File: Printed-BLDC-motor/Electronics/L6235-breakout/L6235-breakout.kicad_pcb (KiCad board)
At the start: 2 copper layers, 55 x 43 mm, 35 parts, among them J1 Conn_01x06_Male, J2 HALL, J3 MOTOR, J5 PWR, U1 L6235PD, U2 L7805

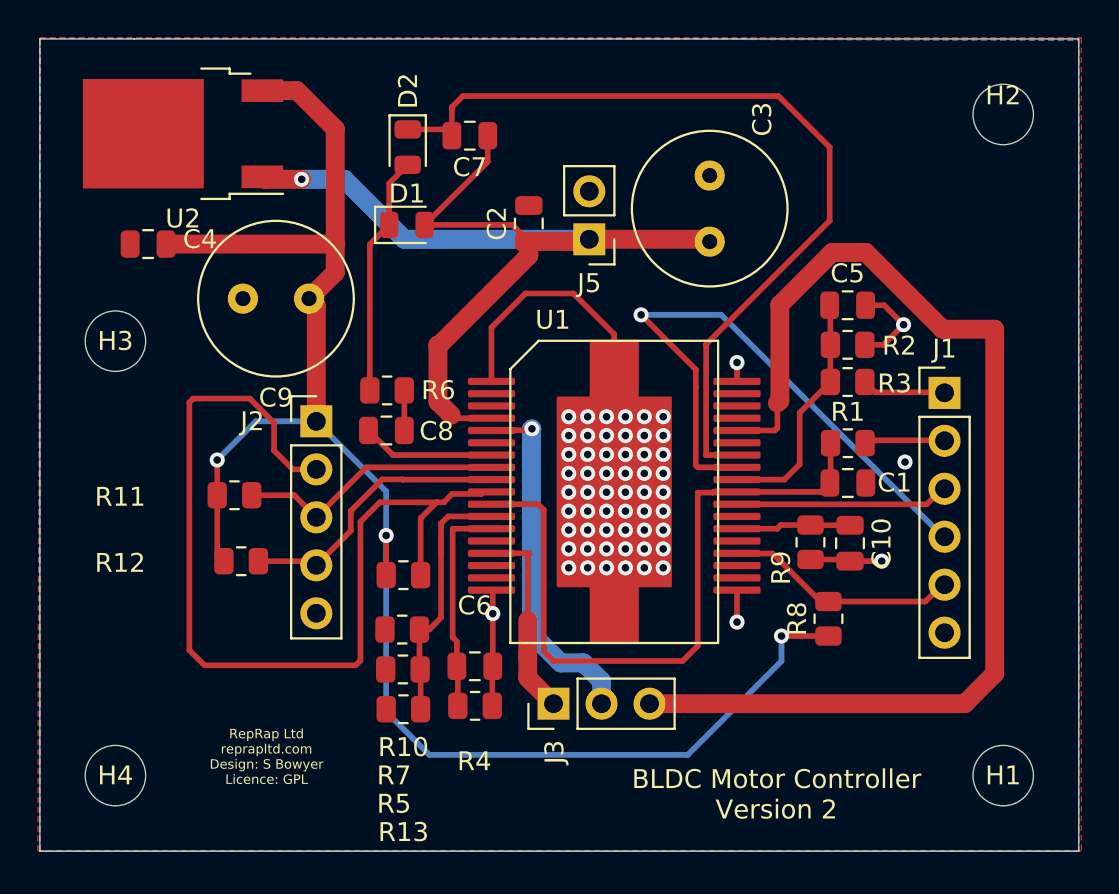
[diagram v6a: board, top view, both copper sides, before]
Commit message: Fixed missing chip connetions.
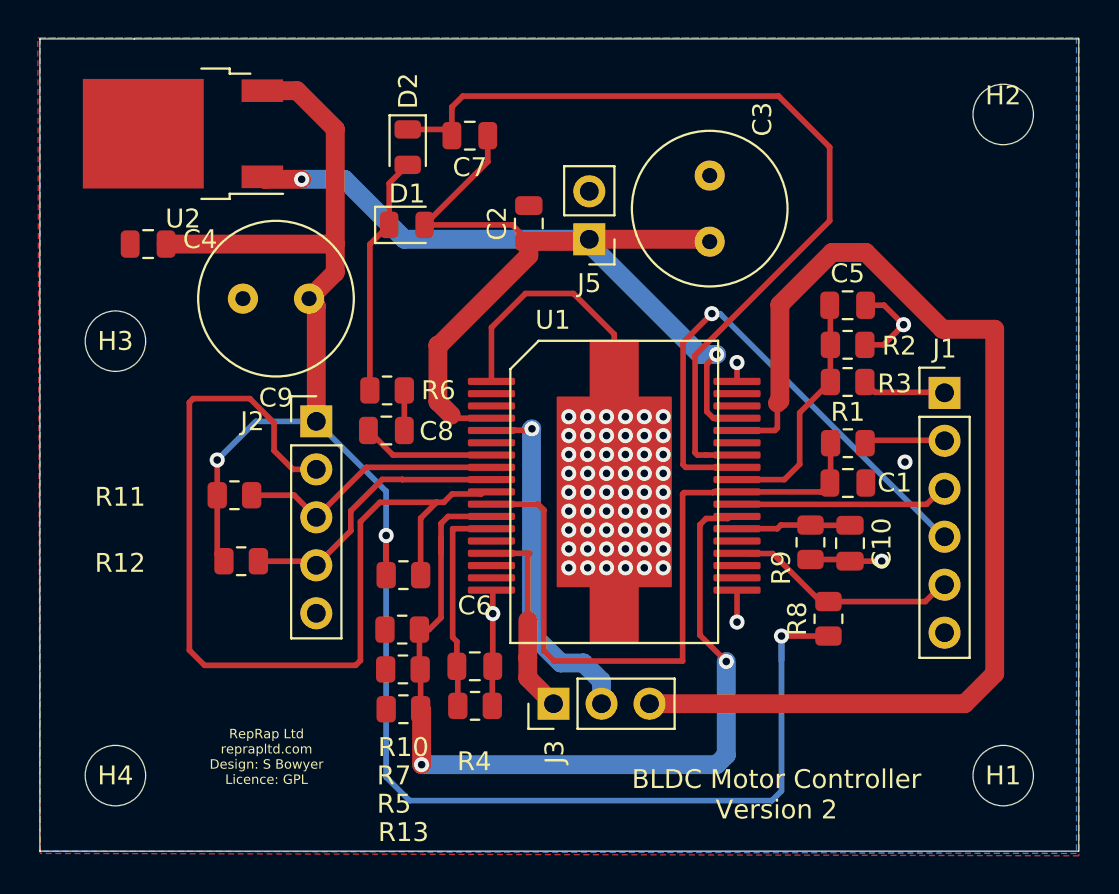
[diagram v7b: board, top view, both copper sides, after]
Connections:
- U1 pad 25: Net-(U1-Pad25) -> Net-(R13-Pad2)
- U1 pad 33: Net-(U1-Pad33) -> VSS
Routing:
- net Net-(R13-Pad2): track 14.2 -> 48.4 mm, vias 0 -> 2
- net VSS: track 54.2 -> 68.6 mm, vias 1 -> 2
- net +5V: track 88.5 -> 97.9 mm
- net BRAKE: track 32.2 -> 28.6 mm
- net Net-(C7-Pad2): track 46.0 -> 46.8 mm

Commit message: V2 PCB send for trial production.
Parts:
- moved D1 26.8 mm to (46.7, 151.6), turned to 270 degrees
- moved D2 22.9 mm to (43.1, 149.1), turned to 0 degrees
- moved C4 20.5 mm to (24.9, 148.3)
- moved J5 18.9 mm to (48.9, 156.3), turned to 0 degrees
- moved C7 15.2 mm to (38.6, 149.1), turned to 0 degrees
- moved H3 13.9 mm to (12.0, 151.0)
- moved U2 13.2 mm to (21.7, 153.2)
- moved C2 7.10 mm to (20.6, 160.0), turned to 180 degrees
- moved H4 7.00 mm to (12.0, 186.0)
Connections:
- net VSS renamed VDD
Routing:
- net Net-(D1-Pad1): track 12.9 -> 39.3 mm, vias 0 -> 2
- net Net-(C7-Pad2): track 46.8 -> 27.3 mm
- net PHASE2: track 19.0 -> 31.9 mm
- net VDD: track 68.6 -> 69.6 mm
- net +5V: track 97.9 -> 98.5 mm, vias 3 -> 4
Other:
- board size 55 x 43 mm -> 48 x 43 mm
- board text added: "+5V"
- board text added: "F/R"
- board text added: "GND"
- board text added: "HALL"
- board text added: "MOTOR"
- board text added: "VDD"
- board text added: "brake"
- board text added: "enable"
- board text added: "speed"
- board text added: "tacho"
